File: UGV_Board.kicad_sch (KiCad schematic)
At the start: 42 parts, among them J1 I2C_EXPANSION, J2 Debug Header, J3 ESP_Header, J4 RFLCTR_Header, J5 RFLCTL_Header, J6 IMU_Daughter_Header, J7 Conn_01x02_Female, J8 Conn_01x02_Female, SW1 SW_MCU_EN, SW2 SW_PICO_RST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

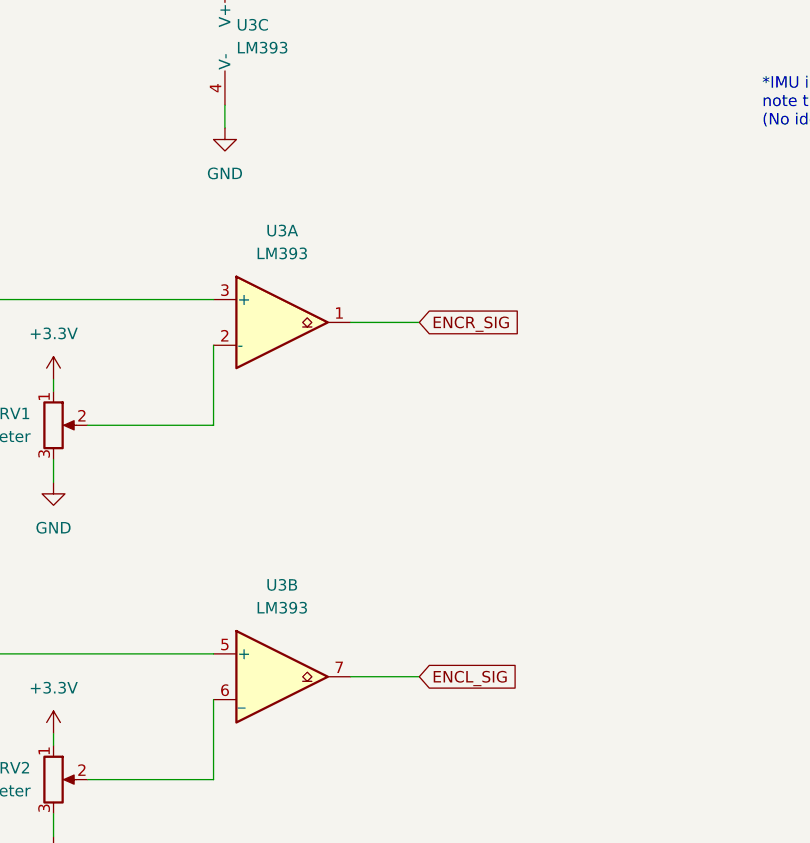
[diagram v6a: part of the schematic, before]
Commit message: Pullups on comparators
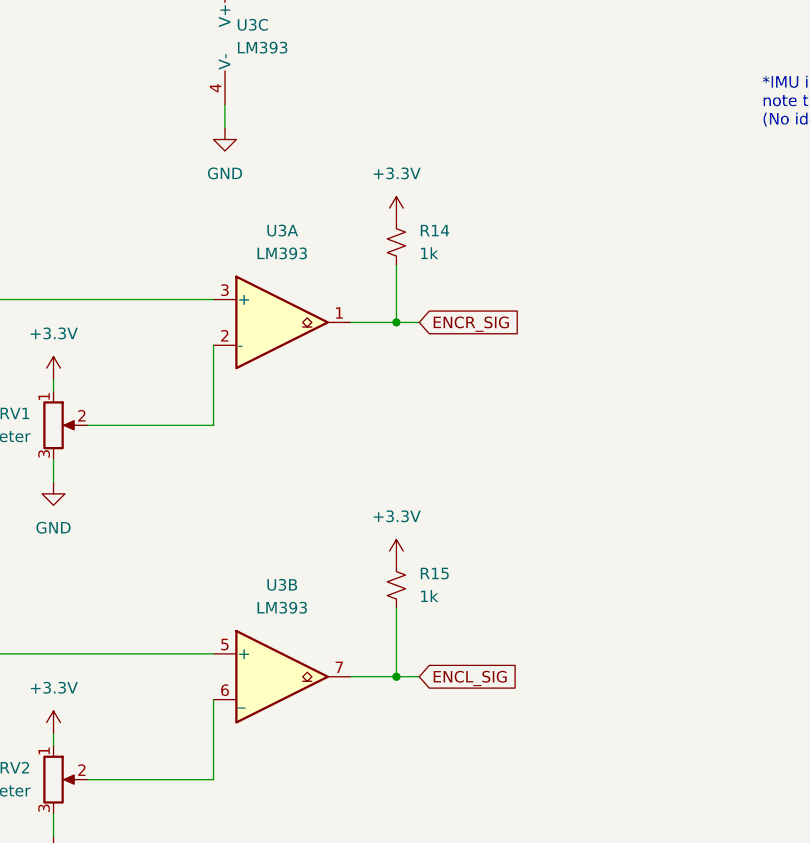
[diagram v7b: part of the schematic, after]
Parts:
- added R14, R15: 1k, Resistor_SMD:R_1206_3216Metric_Pad1.30x1.75mm_HandSolder, symbol Device:R_Small_US
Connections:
- net +3.3V: now also R14.2, R15.2
- net ENCL_SIG: now also R15.1
- net ENCR_SIG: now also R14.1
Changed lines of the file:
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@@
   (junction (at 345.44 124.46) (diameter 0) (color 0 0 0 0)
   )
+  (junction (at 243.84 368.3) (diameter 0) (color 0 0 0 0)
+  )
   (junction (at 341.63 143.51) (diameter 0) (color 0 0 0 0)
   )
@@
   (junction (at 330.2 184.15) (diameter 0) (color 0 0 0 0)
   )
+  (junction (at 243.84 328.93) (diameter 0) (color 0 0 0 0)
+  )
   (junction (at 358.14 127) (diameter 0) (color 0 0 0 0)
   )
@@
     (stroke (width 0) (type default) (color 0 0 0 0))
   )
+  (wire (pts (xy 243.84 328.93) (xy 246.38 328.93))
+    (stroke (width 0) (type default) (color 0 0 0 0))
+  )
   (wire (pts (xy 436.88 215.9) (xy 433.07 215.9))
     (stroke (width 0) (type default) (color 0 0 0 0))
@@
     (stroke (width 0) (type default) (color 0 0 0 0))
   )
+  (wire (pts (xy 243.84 368.3) (xy 246.38 368.3))
+    (stroke (width 0) (type default) (color 0 0 0 0))
+  )
   (wire (pts (xy 284.48 275.59) (xy 289.56 275.59))
     (stroke (width 0) (type default) (color 0 0 0 0))
@@
     (stroke (width 0) (type default) (color 0 0 0 0))
   )
-  (wire (pts (xy 238.76 328.93) (xy 246.38 328.93))
+  (wire (pts (xy 238.76 328.93) (xy 243.84 328.93))
     (stroke (width 0) (type default) (color 0 0 0 0))
   )
@@
     (stroke (width 0) (type default) (color 0 0 0 0))
   )
+  (wire (pts (xy 243.84 322.58) (xy 243.84 328.93))
+    (stroke (width 0) (type default) (color 0 0 0 0))
+  )
   (wire (pts (xy 284.48 273.05) (xy 289.56 273.05))
     (stroke (width 0) (type default) (color 0 0 0 0))
@@
     (stroke (width 0) (type default) (color 0 0 0 0))
   )
+  (wire (pts (xy 243.84 360.68) (xy 243.84 368.3))
+    (stroke (width 0) (type default) (color 0 0 0 0))
+  )
   (wire (pts (xy 323.85 284.48) (xy 323.85 287.02))
     (stroke (width 0) (type default) (color 0 0 0 0))
@@
     (stroke (width 0) (type default) (color 0 0 0 0))
   )
-  (wire (pts (xy 238.76 368.3) (xy 246.38 368.3))
+  (wire (pts (xy 238.76 368.3) (xy 243.84 368.3))
     (stroke (width 0) (type default) (color 0 0 0 0))
   )
@@
     (pin "4")
   )
+  (symbol (lib_id "Device:R_Small_US") (at 243.84 358.14 180) (unit 1)
+    (in_bom yes) (on_board yes) (fields_autoplaced)
+    (property "Reference" "R15" (id 0) (at 246.38 356.8699 0)
+      (effects (font (size 1.27 1.27)) (justify right))
+    )
+    (property "Value" "1k" (id 1) (at 246.38 359.4099 0)
+      (effects (font (size 1.27 1.27)) (justify right))
+    )
+    (property "Footprint" "Resistor_SMD:R_1206_3216Metric_Pad1.30x1.75mm_HandSolder" (id 2) (at 243.84 358.14 0)
+      (effects (font (size 1.27 1.27)) hide)
+    )
+    (property "Datasheet" "~" (id 3) (at 243.84 358.14 0)
+      (effects (font (size 1.27 1.27)) hide)
+    )
+    (pin "1")
+    (pin "2")
+  )
   (symbol (lib_id "power:+6V") (at 356.87 186.69 90) (unit 1)
     (in_bom yes) (on_board yes) (fields_autoplaced)
@@
     )
     (property "Datasheet" "~" (id 3) (at 427.99 226.06 0)
+      (effects (font (size 1.27 1.27)) hide)
+    )
+    (pin "1")
+    (pin "2")
+  )
+  (symbol (lib_id "Device:R_Small_US") (at 243.84 320.04 180) (unit 1)
+    (in_bom yes) (on_board yes) (fields_autoplaced)
+    (property "Reference" "R14" (id 0) (at 246.38 318.7699 0)
+      (effects (font (size 1.27 1.27)) (justify right))
+    )
+    (property "Value" "1k" (id 1) (at 246.38 321.3099 0)
+      (effects (font (size 1.27 1.27)) (justify right))
+    )
+    (property "Footprint" "Resistor_SMD:R_1206_3216Metric_Pad1.30x1.75mm_HandSolder" (id 2) (at 243.84 320.04 0)
+      (effects (font (size 1.27 1.27)) hide)
+    )
+    (property "Datasheet" "~" (id 3) (at 243.84 320.04 0)
       (effects (font (size 1.27 1.27)) hide)
     )
@@
     (pin "8")
   )
+  (symbol (lib_name "+3.3V_7") (lib_id "power:+3.3V") (at 243.84 355.6 0) (unit 1)
+    (in_bom yes) (on_board yes) (fields_autoplaced)
+    (property "Reference" "#PWR0134" (id 0) (at 243.84 359.41 0)
+      (effects (font (size 1.27 1.27)) hide)
+    )
+    (property "Value" "+3.3V" (id 1) (at 243.84 350.52 0))
+    (property "Footprint" "" (id 2) (at 243.84 355.6 0)
+      (effects (font (size 1.27 1.27)) hide)
+    )
+    (property "Datasheet" "" (id 3) (at 243.84 355.6 0)
+      (effects (font (size 1.27 1.27)) hide)
+    )
+    (pin "1")
+  )
   (symbol (lib_id "Connector:Conn_01x04_Female") (at 170.18 323.85 180) (unit 1)
     (in_bom yes) (on_board yes)
@@
     (pin "3")
     (pin "4")
+  )
+  (symbol (lib_name "+3.3V_7") (lib_id "power:+3.3V") (at 243.84 317.5 0) (unit 1)
+    (in_bom yes) (on_board yes) (fields_autoplaced)
+    (property "Reference" "#PWR0137" (id 0) (at 243.84 321.31 0)
+      (effects (font (size 1.27 1.27)) hide)
+    )
+    (property "Value" "+3.3V" (id 1) (at 243.84 312.42 0))
+    (property "Footprint" "" (id 2) (at 243.84 317.5 0)
+      (effects (font (size 1.27 1.27)) hide)
+    )
+    (property "Datasheet" "" (id 3) (at 243.84 317.5 0)
+      (effects (font (size 1.27 1.27)) hide)
+    )
+    (pin "1")
   )
   (symbol (lib_id "Device:R_Small_US") (at 177.8 330.2 180) (unit 1)
@@
       (reference "#PWR0133") (unit 1) (value "GND") (footprint "")
     )
+    (path "/afb9d668-050d-4733-ad03-80c189bfe1fa"
+      (reference "#PWR0134") (unit 1) (value "+3.3V") (footprint "")
+    )
     (path "/8a73a5c8-b6b2-4b9f-a45b-d6aa4f2ccad5"
       (reference "#PWR0135") (unit 1) (value "+7.5V") (footprint "")
@@
       (reference "#PWR0136") (unit 1) (value "GND") (footprint "")
     )
+    (path "/b5578900-d8bc-43b8-97d9-e56d4e20b73b"
+      (reference "#PWR0137") (unit 1) (value "+3.3V") (footprint "")
+    )
     (path "/8e5869e2-bbd2-4bca-8704-5fa8462ff71f"
       (reference "C1") (unit 1) (value "10uF") (footprint "Capacitor_SMD:C_1206_3216Metric_Pad1.33x1.80mm_HandSolder")
@@
       (reference "R13") (unit 1) (value "10k") (footprint "Resistor_SMD:R_1206_3216Metric_Pad1.30x1.75mm_HandSolder")
     )
+    (path "/6993201a-3348-485d-9f9e-b7c0fc9944b9"
+      (reference "R14") (unit 1) (value "1k") (footprint "Resistor_SMD:R_1206_3216Metric_Pad1.30x1.75mm_HandSolder")
+    )
+    (path "/478c6a0b-6f16-4756-a544-87f0475ab727"
+      (reference "R15") (unit 1) (value "1k") (footprint "Resistor_SMD:R_1206_3216Metric_Pad1.30x1.75mm_HandSolder")
+    )
     (path "/2e81d893-382c-40d5-9de5-38cb4560c275"
